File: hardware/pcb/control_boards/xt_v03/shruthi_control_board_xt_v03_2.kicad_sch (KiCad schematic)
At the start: 39 parts, among them IC4 4051N, IC5 4051N, IC6 4051N, IC7 4051N

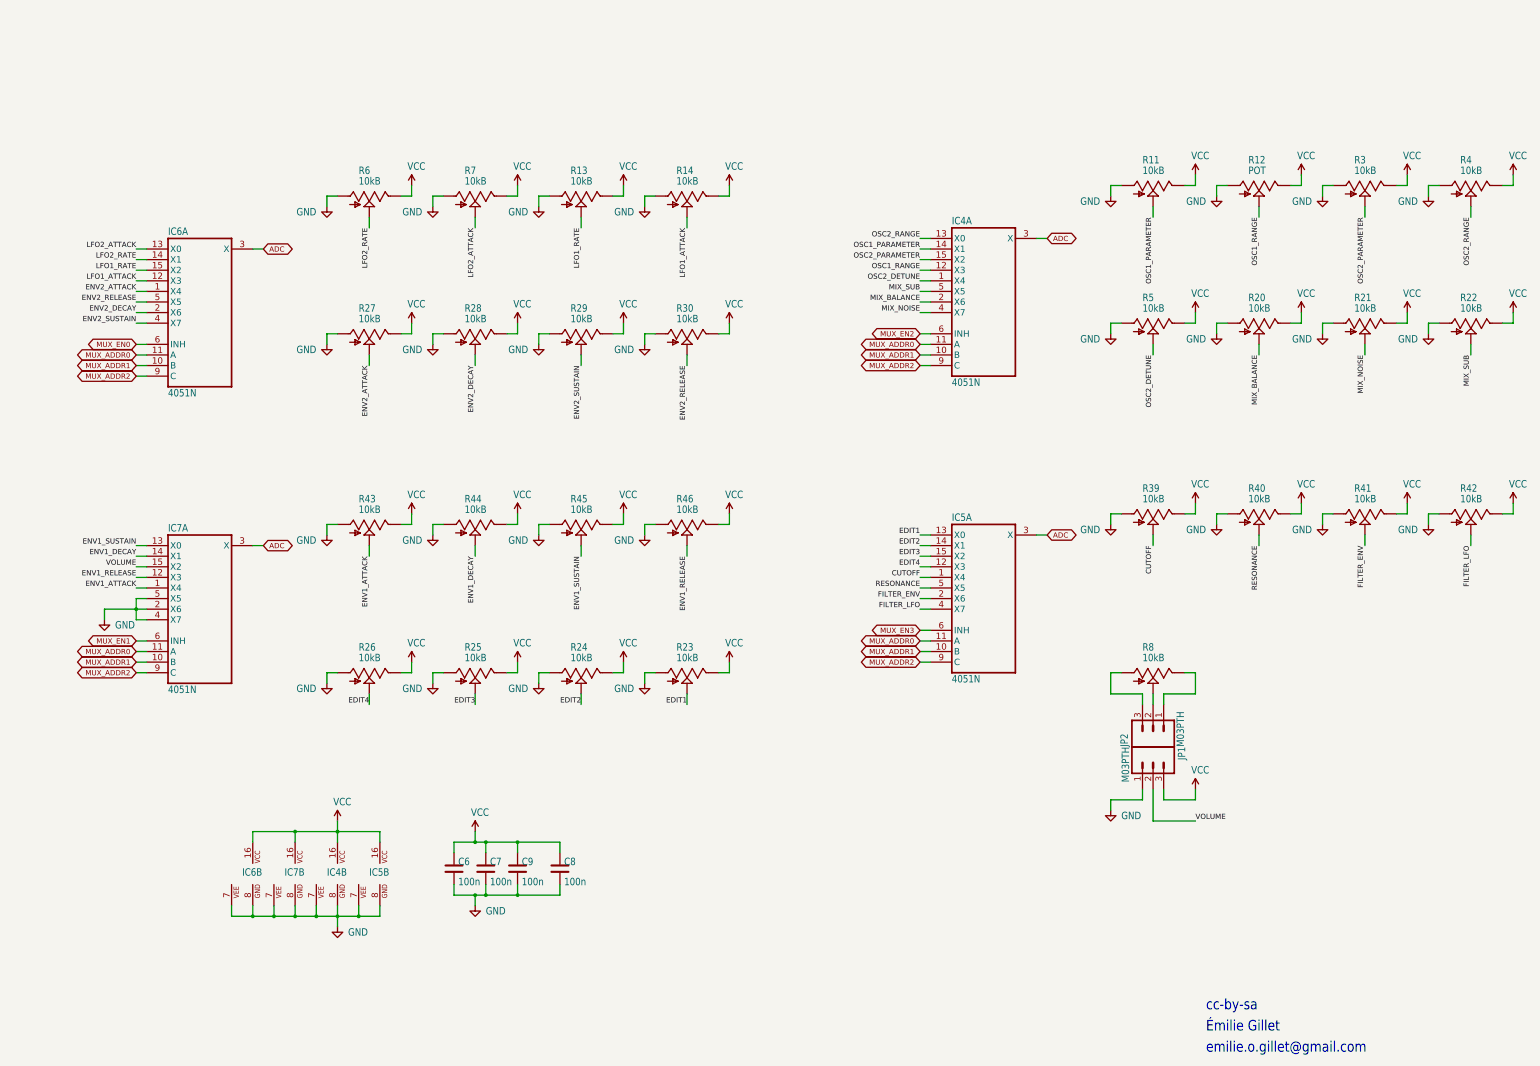
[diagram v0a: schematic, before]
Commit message: update 4051 to use kicad symbols
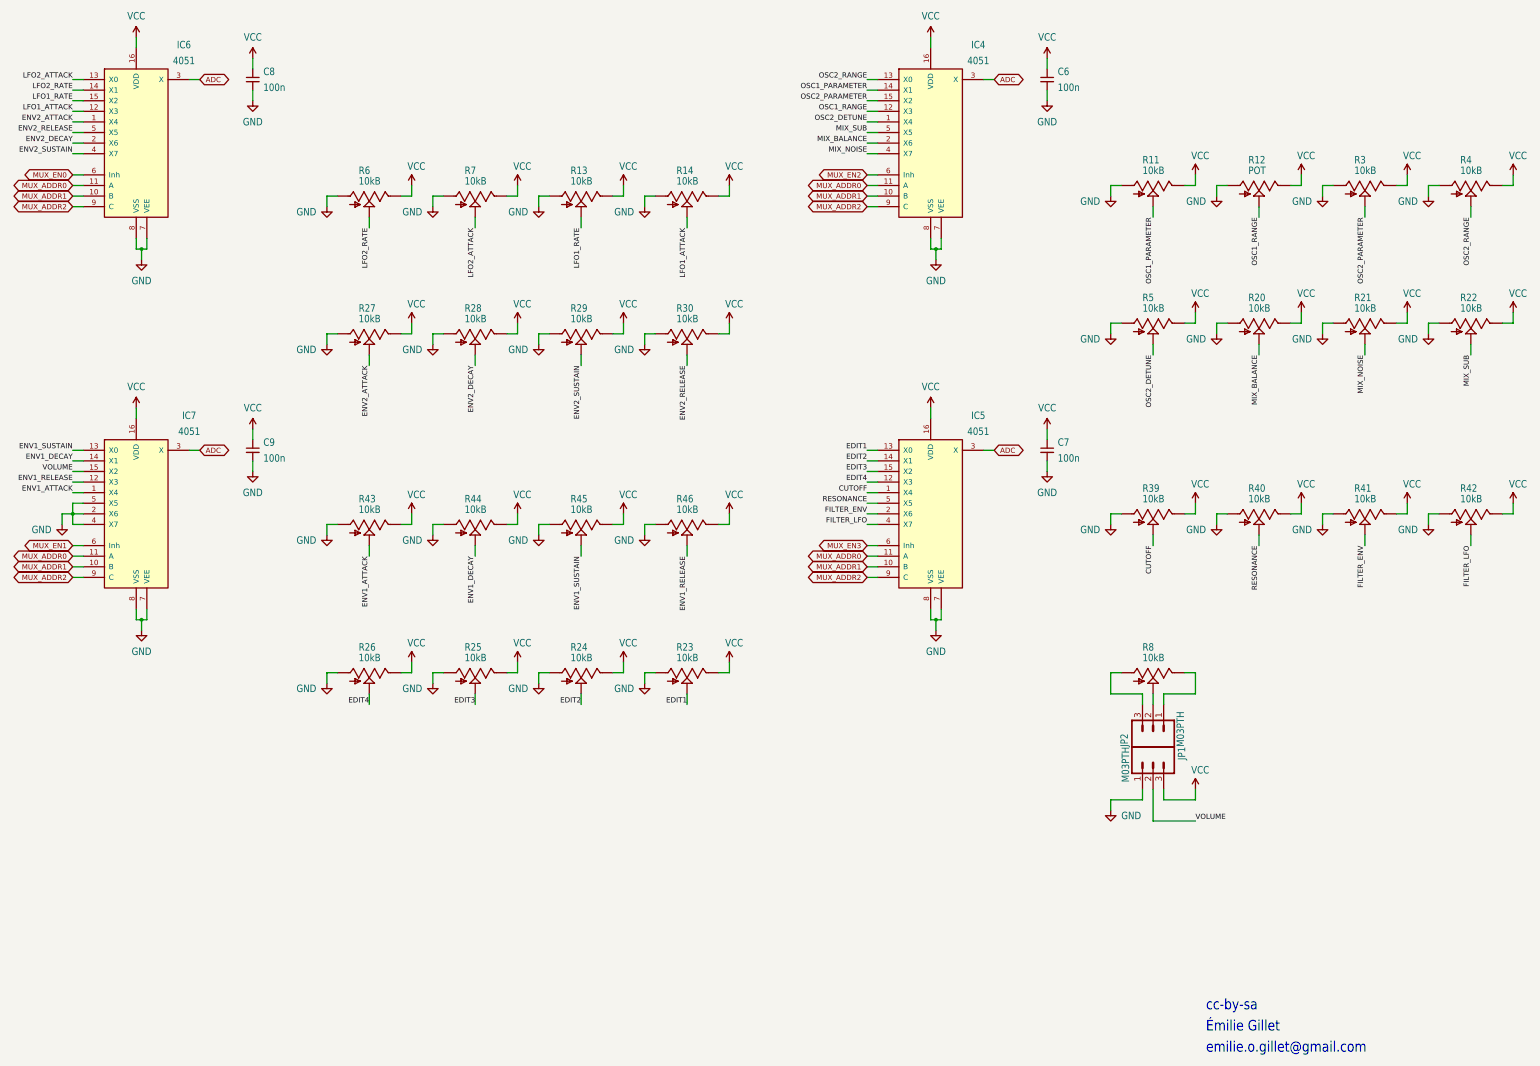
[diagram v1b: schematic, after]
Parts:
- removed unit 2 of IC4
- removed unit 2 of IC5
- removed unit 2 of IC6
- removed unit 2 of IC7
- C6, C7, C8, C9: symbol Device:C -> Device:C_Small
- IC4, IC5, IC6, IC7: value 4051N -> 4051; symbol shruthi_control_board_xt_v03-eagle-import:4051N -> 4xxx:4051
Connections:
- net GND: now also IC4.7 (VEE), IC4.8 (VSS), IC5.7 (VEE), IC5.8 (VSS), IC6.7 (VEE), IC6.8 (VSS), IC7.7 (VEE), IC7.8 (VSS)
- net VCC: now also IC4.16 (VDD), IC5.16 (VDD), IC6.16 (VDD), IC7.16 (VDD)
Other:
- moved on the sheet: C6, C7, C8, C9

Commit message: update 4051 footprints
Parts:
- IC4, IC5, IC6, IC7: footprint shruthi_control_board_xt_v03:DIL16 -> Package_DIP:DIP-16_W7.62mm_Socket_LongPads
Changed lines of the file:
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@@
 			)
 		)
-		(property "Footprint" "shruthi_control_board_xt_v03:DIL16"
+		(property "Footprint" "Package_DIP:DIP-16_W7.62mm_Socket_LongPads"
 			(at 50.8 139.7 0)
 			(effects
@@
 			)
 		)
-		(property "Footprint" "shruthi_control_board_xt_v03:DIL16"
+		(property "Footprint" "Package_DIP:DIP-16_W7.62mm_Socket_LongPads"
 			(at 241.3 139.7 0)
 			(effects
@@
 			)
 		)
-		(property "Footprint" "shruthi_control_board_xt_v03:DIL16"
+		(property "Footprint" "Package_DIP:DIP-16_W7.62mm_Socket_LongPads"
 			(at 241.3 50.8 0)
 			(effects
@@
 			)
 		)
-		(property "Footprint" "shruthi_control_board_xt_v03:DIL16"
+		(property "Footprint" "Package_DIP:DIP-16_W7.62mm_Socket_LongPads"
 			(at 50.8 50.8 0)
 			(effects

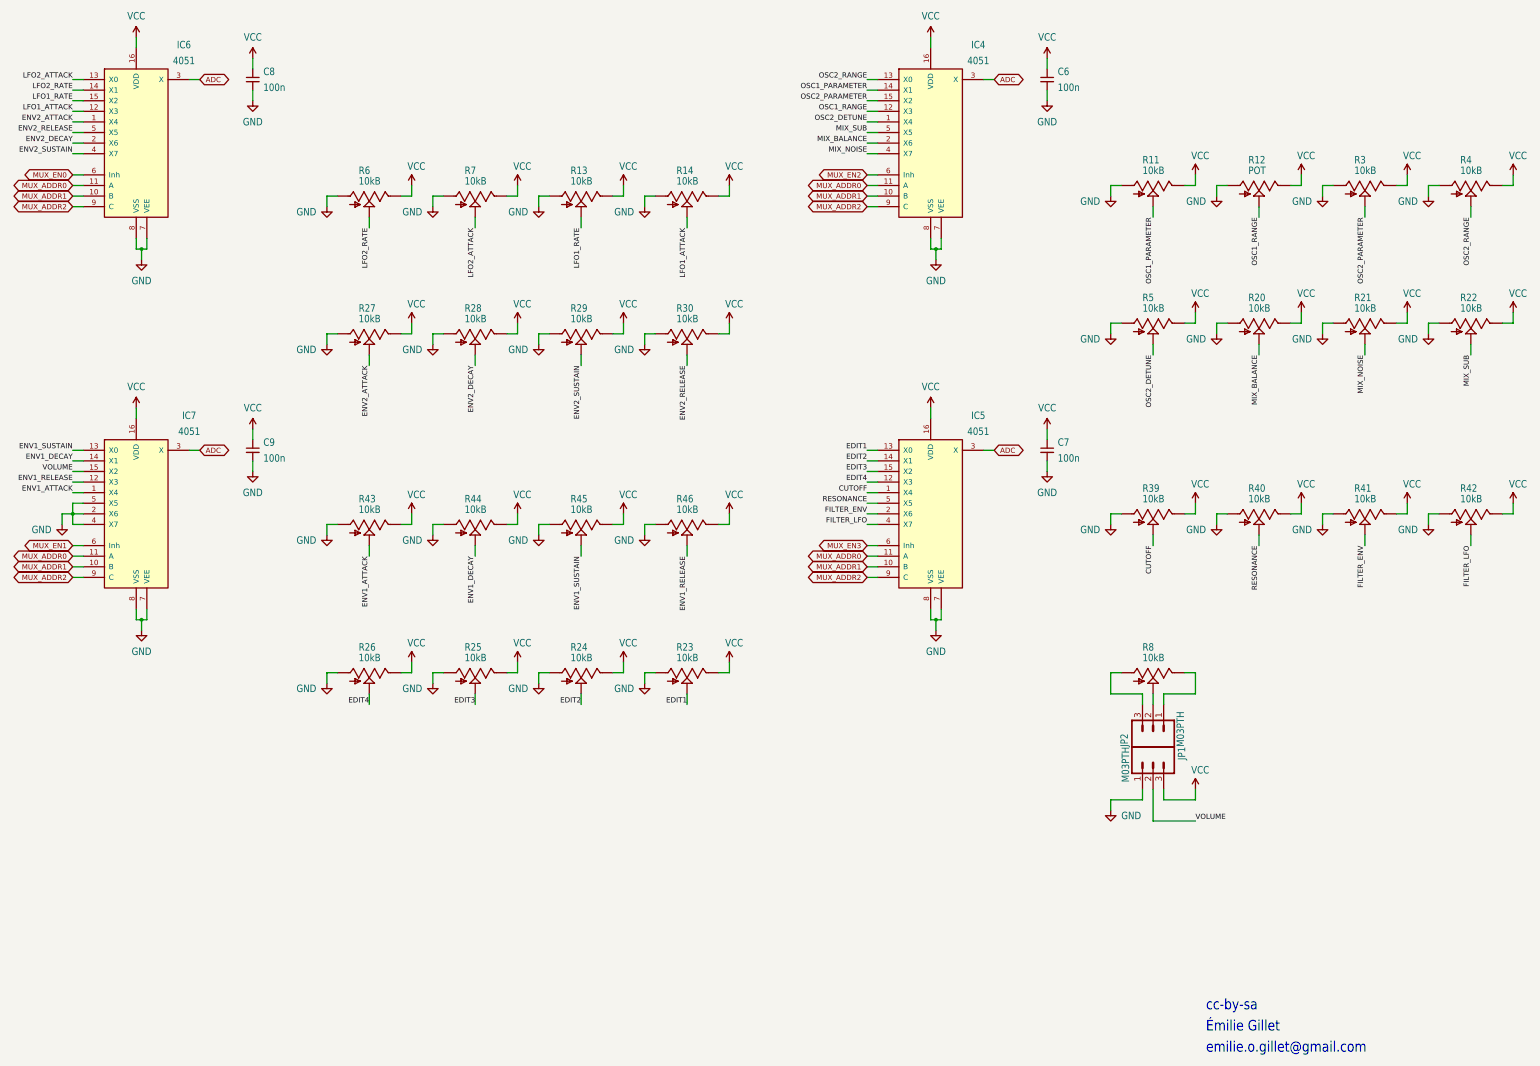
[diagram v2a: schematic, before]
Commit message: update pots to use kicad symbols
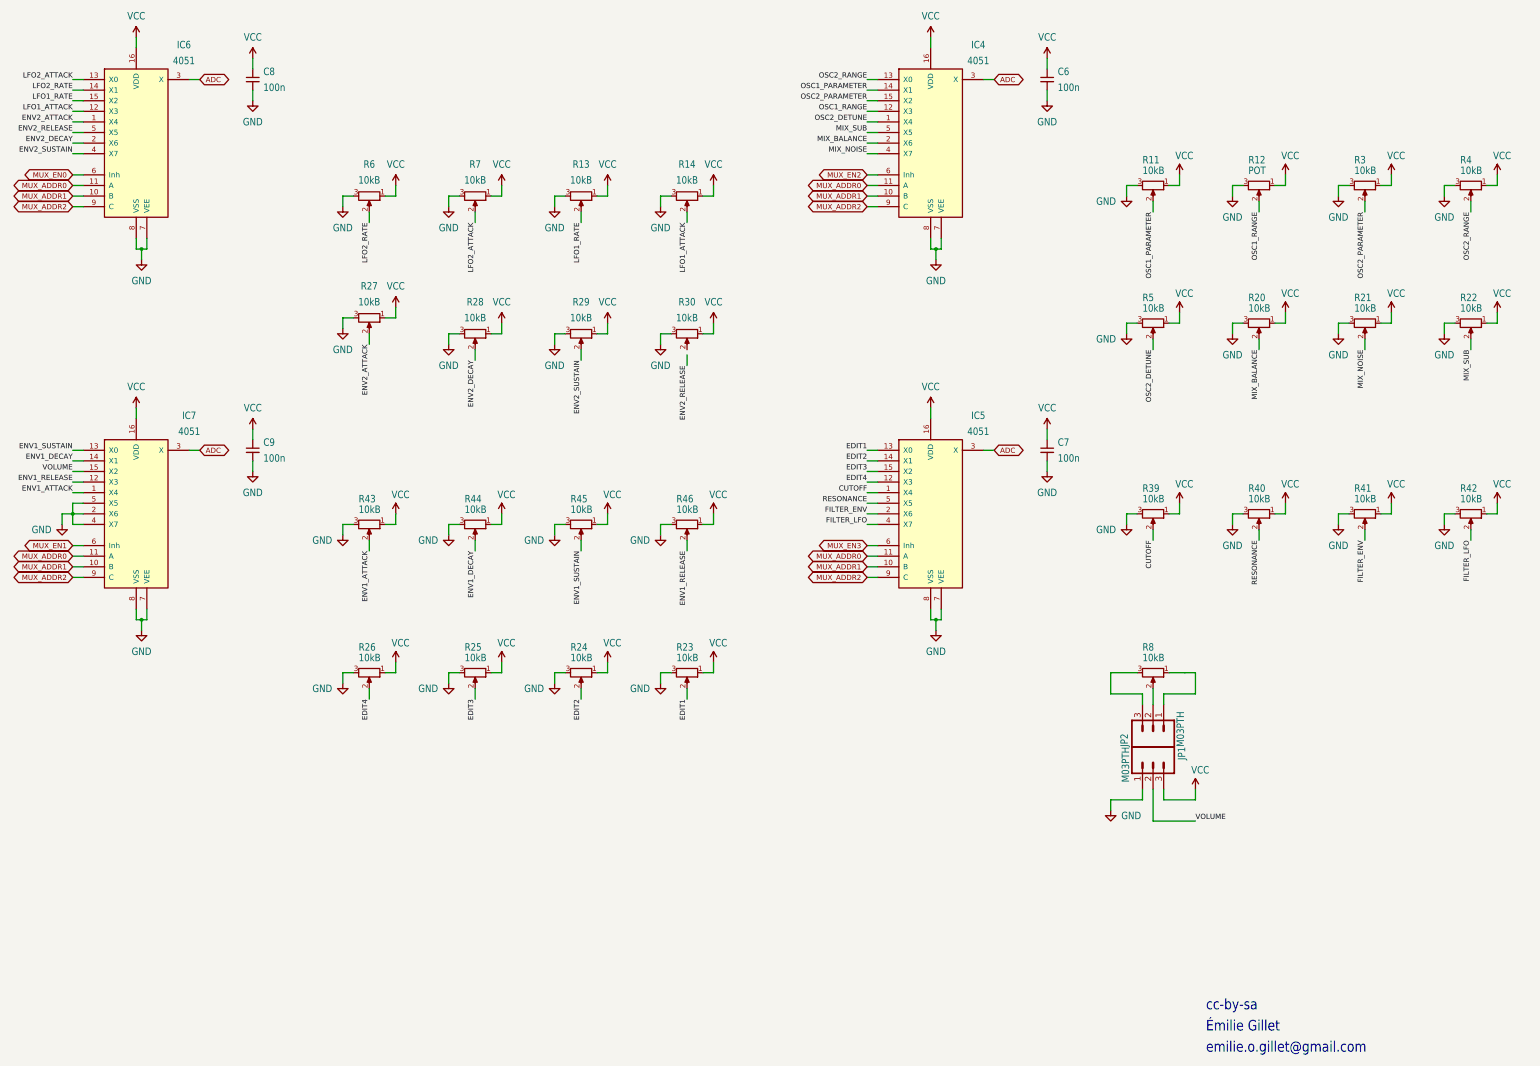
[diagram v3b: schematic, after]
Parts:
- R11, R12, R13, R14, R20, R21, R22, R23, R24, R25, R26, R27, R28, R29, R3, R30, R39, R4, R40, R41, R42, R43, R44, R45, R46, R5, R6, R7, R8: symbol shruthi_control_board_xt_v03-eagle-import:POT_USVERTICAL -> Device:R_Potentiometer
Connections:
- net CUTOFF: now also R39.2; no longer R39.P$2 (S)
- net EDIT1: now also R23.2; no longer R23.P$2 (S)
- net EDIT2: now also R24.2; no longer R24.P$2 (S)
- net EDIT3: now also R25.2; no longer R25.P$2 (S)
- net EDIT4: now also R26.2; no longer R26.P$2 (S)
- net ENV1_ATTACK: now also R43.2; no longer R43.P$2 (S)
- net ENV1_DECAY: now also R44.2; no longer R44.P$2 (S)
- net ENV1_RELEASE: now also R46.2; no longer R46.P$2 (S)
- net ENV1_SUSTAIN: now also R45.2; no longer R45.P$2 (S)
- net ENV2_ATTACK: now also R27.2; no longer R27.P$2 (S)
- net ENV2_DECAY: now also R28.2; no longer R28.P$2 (S)
- net ENV2_RELEASE: no longer R30.P$2 (S)
- net ENV2_SUSTAIN: now also R29.2; no longer R29.P$2 (S)
- net FILTER_ENV: now also R41.2; no longer R41.P$2 (S)
- net FILTER_LFO: now also R42.2; no longer R42.P$2 (S)
- net GND: now also R11.3, R12.3, R13.3, R14.3, R20.3, R21.3, R22.3, R23.3, R24.3, R25.3, R26.3, R27.3, R28.3, R29.3, R3.3, R30.3, R39.3, R4.3, R40.3, R41.3, R42.3, R43.3, R44.3, R45.3, R46.3, R5.3, R6.3, R7.3; no longer R11.P$3 (A), R12.P$3 (A), R13.P$3 (A), R14.P$3 (A), R20.P$3 (A), R21.P$3 (A), R22.P$3 (A), R23.P$3 (A), R24.P$3 (A), R25.P$3 (A), R26.P$3 (A), R27.P$3 (A), R28.P$3 (A), R29.P$3 (A), R3.P$3 (A), R30.P$3 (A), R39.P$3 (A), R4.P$3 (A), R40.P$3 (A), R41.P$3 (A), R42.P$3 (A), R43.P$3 (A), R44.P$3 (A), R45.P$3 (A), R46.P$3 (A), R5.P$3 (A), R6.P$3 (A), R7.P$3 (A)
- net LFO1_ATTACK: now also R14.2; no longer R14.P$2 (S)
- net LFO1_RATE: now also R13.2; no longer R13.P$2 (S)
- net LFO2_ATTACK: now also R7.2; no longer R7.P$2 (S)
- net LFO2_RATE: now also R6.2; no longer R6.P$2 (S)
- net MIX_BALANCE: now also R20.2; no longer R20.P$2 (S)
- net MIX_NOISE: now also R21.2; no longer R21.P$2 (S)
- net MIX_SUB: now also R22.2; no longer R22.P$2 (S)
- net OSC1_PARAMETER: now also R11.2; no longer R11.P$2 (S)
- net OSC1_RANGE: now also R12.2; no longer R12.P$2 (S)
- net OSC2_DETUNE: now also R5.2; no longer R5.P$2 (S)
- net OSC2_PARAMETER: now also R3.2; no longer R3.P$2 (S)
- net OSC2_RANGE: now also R4.2; no longer R4.P$2 (S)
- net RESONANCE: now also R40.2; no longer R40.P$2 (S)
- net VCC: now also R11.1, R12.1, R13.1, R14.1, R20.1, R21.1, R22.1, R23.1, R24.1, R25.1, R26.1, R27.1, R28.1, R29.1, R3.1, R30.1, R39.1, R4.1, R40.1, R41.1, R42.1, R43.1, R44.1, R45.1, R46.1, R5.1, R6.1, R7.1; no longer R11.P$1 (E), R12.P$1 (E), R13.P$1 (E), R14.P$1 (E), R20.P$1 (E), R21.P$1 (E), R22.P$1 (E), R23.P$1 (E), R24.P$1 (E), R25.P$1 (E), R26.P$1 (E), R27.P$1 (E), R28.P$1 (E), R29.P$1 (E), R3.P$1 (E), R30.P$1 (E), R39.P$1 (E), R4.P$1 (E), R40.P$1 (E), R41.P$1 (E), R42.P$1 (E), R43.P$1 (E), R44.P$1 (E), R45.P$1 (E), R46.P$1 (E), R5.P$1 (E), R6.P$1 (E), R7.P$1 (E)
- net at JP2.1: now also R8.1; no longer R8.P$1 (E)
- net at JP2.2: now also R8.2; no longer R8.P$2 (S)
- net at JP2.3: now also R8.3; no longer R8.P$3 (A)

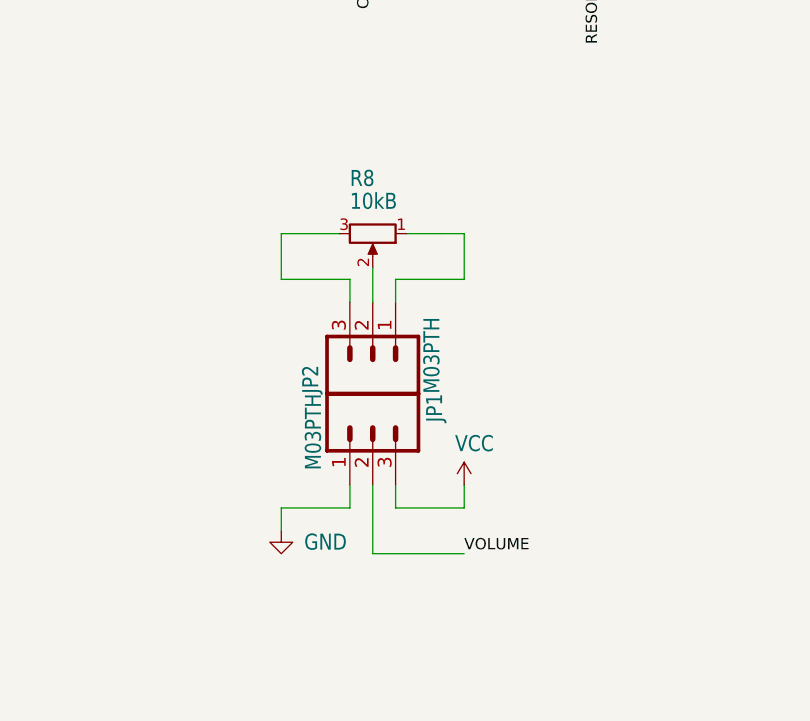
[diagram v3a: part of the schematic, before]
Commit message: update volume jumpers to use kicad symbols
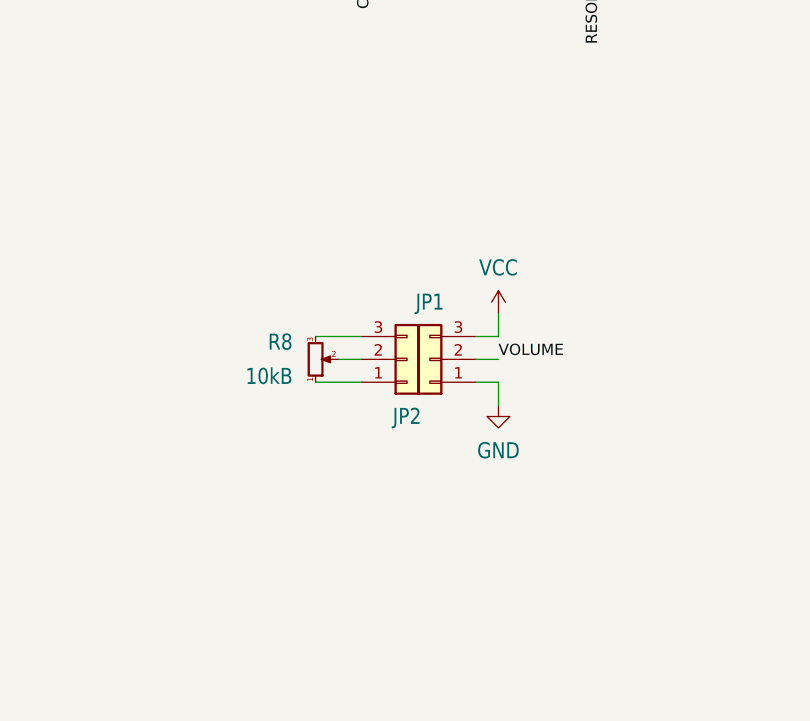
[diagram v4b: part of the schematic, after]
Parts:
- JP1, JP2: symbol shruthi_control_board_xt_v03-eagle-import:M03PTH -> Connector_Generic:Conn_01x03
- R8: symbol Device:R_Potentiometer -> Device:R_Potentiometer_Small
